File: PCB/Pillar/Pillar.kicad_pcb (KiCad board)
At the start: 2 copper layers, 100 x 86.6 mm, 26 parts, among them CN1 GROVE_IIC_5V, CN2 GROVE_IIC_5V, CN3 USB_A, CN4 AudioJack3_SwitchTR, CN5 Micro_SD_Card_Det_Hirose_DM3AT, J1 Speaker, SW1 MDOE, U1 SeeeduinoXIAO, U2 DFPlayerMini, U3 OLED_128x64_IIC

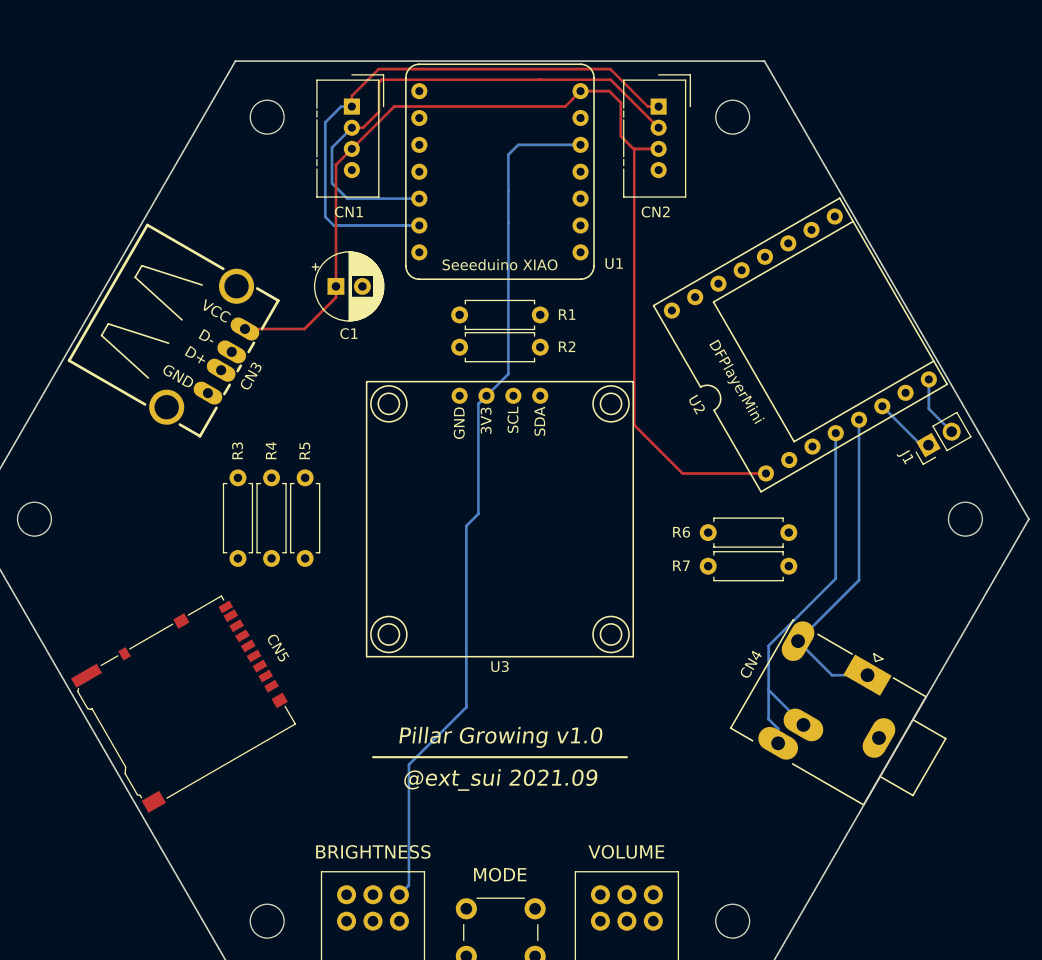
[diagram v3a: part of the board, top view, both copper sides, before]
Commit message: (Pcb) OLED, XIAO のフットプリントに情報を追加して位置を再調整 #60
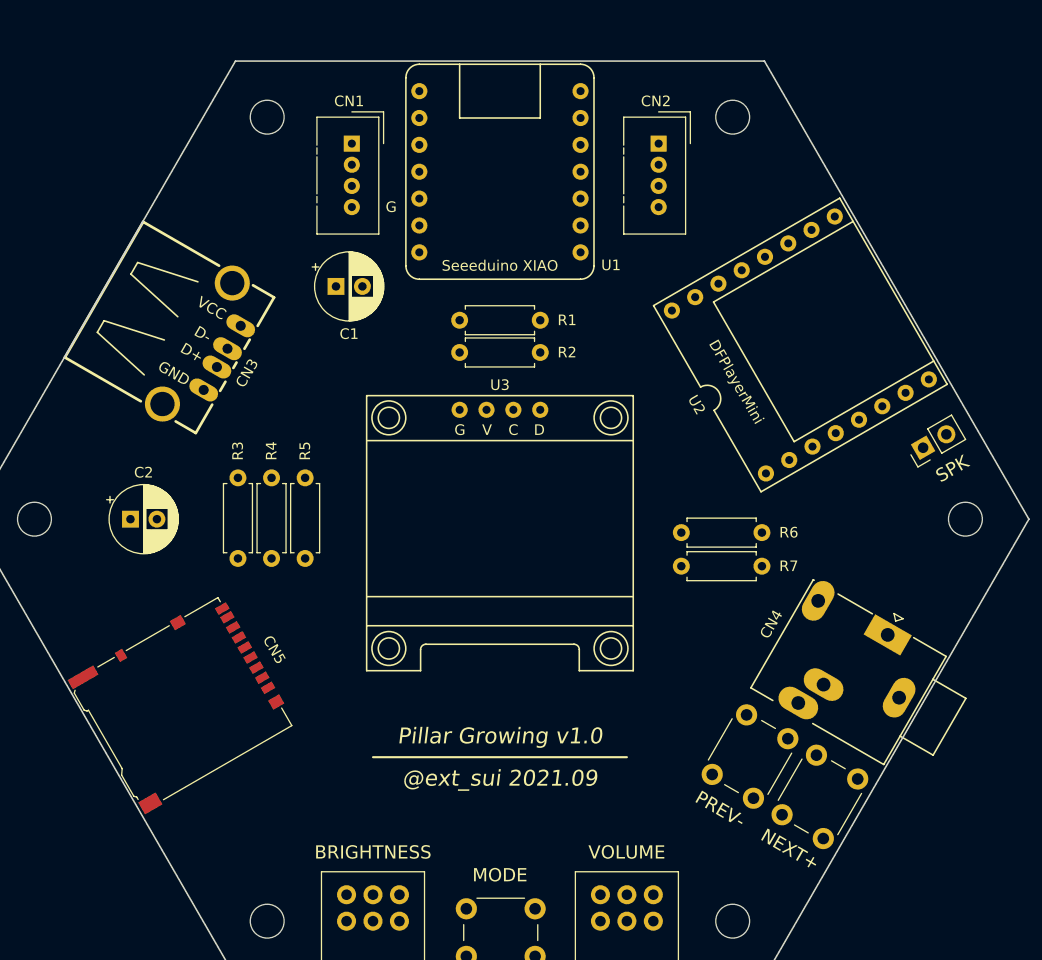
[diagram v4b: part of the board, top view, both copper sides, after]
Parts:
- added C2: 100u, Capacitor_THT:CP_Radial_D6.3mm_P2.50mm, F.Cu at (95.1, 105.0)
- added SW2: NEXT/VOL+, Button_Switch_THT:SW_PUSH_6mm_H8.5mm, F.Cu at (156.7, 132.9)
- added SW3: PREV/VOL-, Button_Switch_THT:SW_PUSH_6mm_H8.5mm, F.Cu at (150.1, 129.1)
- moved CN4 4.26 mm to (166.7, 115.9)
- moved CN1 3.50 mm to (116.0, 69.5)
- moved CN2 3.50 mm to (145.0, 69.5)
- moved R6 2.54 mm to (147.1, 106.3)
- moved R7 2.54 mm to (147.1, 109.4)
- moved U3 1.32 mm to (130.0, 93.3)
- moved J1 0.56 mm to (170.0, 98.2)
- moved R1 0.50 mm to (133.8, 86.2)
- moved R2 0.50 mm to (133.8, 89.2)
- moved CN3 0.50 mm to (101.4, 88.4)
- moved CN5 0.36 mm to (100.0, 122.4)
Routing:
- net 5V: track 100.3 -> 0.00 mm
- net 3V3: track 82.4 -> 0.00 mm
- net SCL: track 53.8 -> 0.00 mm
- net SDA: track 49.3 -> 0.00 mm
- net Net-(CN4-PadR): track 37.0 -> 0.00 mm
- net Net-(CN4-PadT): track 31.2 -> 0.00 mm
- net Net-(J1-Pad1): track 5.88 -> 0.00 mm
- net Net-(J1-Pad2): track 5.83 -> 0.00 mm
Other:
- board text added: "C"
- board text added: "D"
- board text added: "G"
- board text added: "NEXT+"
- board text added: "PREV-"
- board text added: "SPK"
- board text added: "V"
- board text removed: "3V3"
- board text removed: "GND"
- board text removed: "SCL"
- board text removed: "SDA"

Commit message: (Pcb) 配線第0版作成 #60
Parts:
- moved R6 7.62 mm to (154.8, 106.3), turned to 180 degrees
- moved R7 7.62 mm to (154.8, 109.4), turned to 180 degrees
- moved R3 6.35 mm to (111.6, 101.1)
- moved R5 6.35 mm to (105.2, 101.1)
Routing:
- net GND: track 0.00 -> 198.8 mm
- net 3V3: track 0.00 -> 172.6 mm
- net 5V: track 0.00 -> 120.9 mm
- net RV_V: track 0.00 -> 94.7 mm
- net Net-(SW1-Pad1): track 0.00 -> 86.9 mm
- net MOSI: track 0.00 -> 86.6 mm
- net MISO: track 0.00 -> 85.5 mm
- net SCK: track 0.00 -> 75.7 mm, vias 0 -> 1
- net SDA: track 0.00 -> 75.2 mm
- net RV_B: track 0.00 -> 71.4 mm
- net SCL: track 0.00 -> 68.3 mm
- net Net-(SW2-Pad1): track 0.00 -> 66.8 mm
- net Net-(SW3-Pad1): track 0.00 -> 58.6 mm
- net CS: track 0.00 -> 57.1 mm
- net TXD: track 0.00 -> 46.0 mm, vias 0 -> 1
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
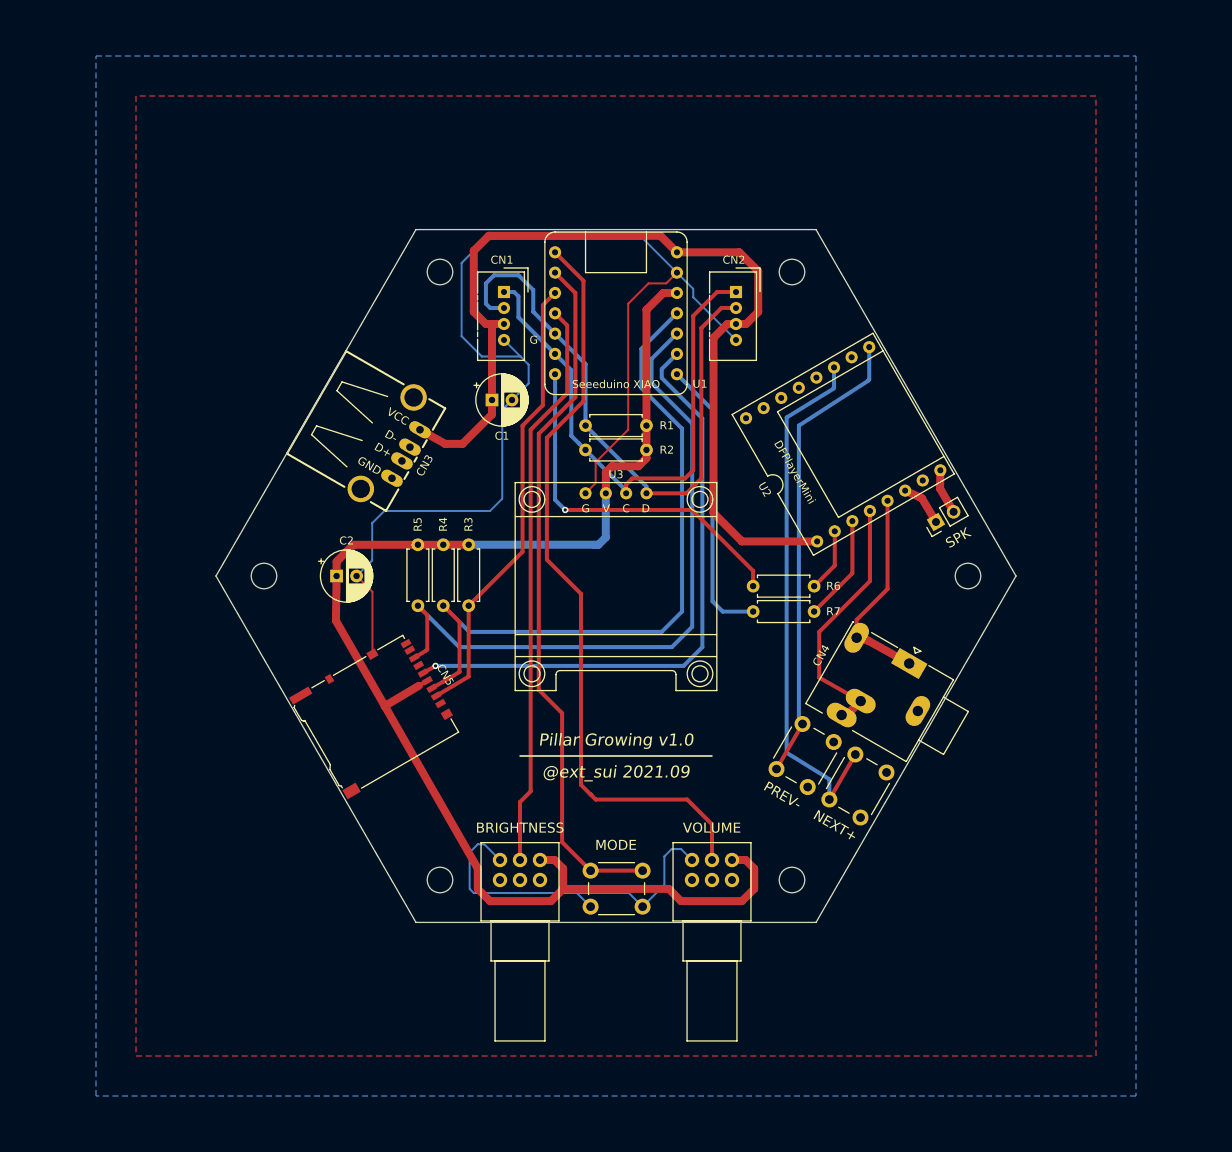
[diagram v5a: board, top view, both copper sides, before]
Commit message: (Pcb) 配線改善：3V3 ラインの直線化と外周 GND 打ち #60
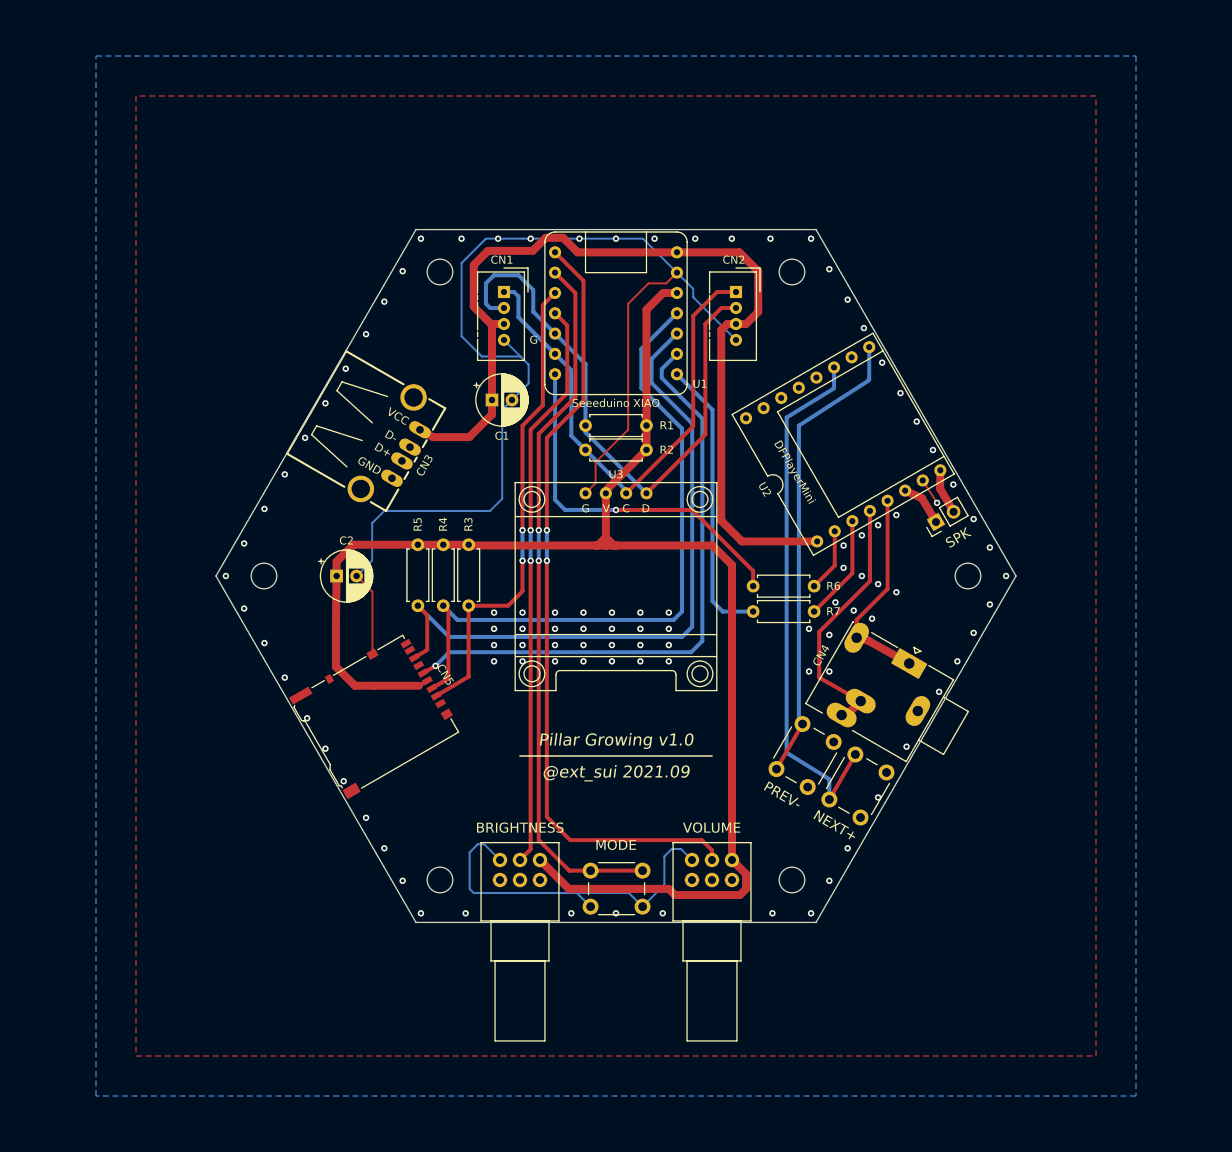
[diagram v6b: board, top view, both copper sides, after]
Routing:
- net 3V3: track 172.6 -> 185.8 mm
- net SCL: track 68.3 -> 64.5 mm
- net GND: track 198.8 -> 202.2 mm, vias 0 -> 100
- net 5V: track 120.9 -> 117.9 mm
- net SDA: track 75.2 -> 72.3 mm
- net RV_V: track 94.7 -> 97.6 mm, vias 0 -> 2
- net CS: track 57.1 -> 60.0 mm, vias 0 -> 2
- net MOSI: track 86.6 -> 84.0 mm
- net Net-(SW1-Pad1): track 86.9 -> 88.4 mm, vias 0 -> 2
- net MISO: track 85.5 -> 84.4 mm
- net RV_B: vias 0 -> 2

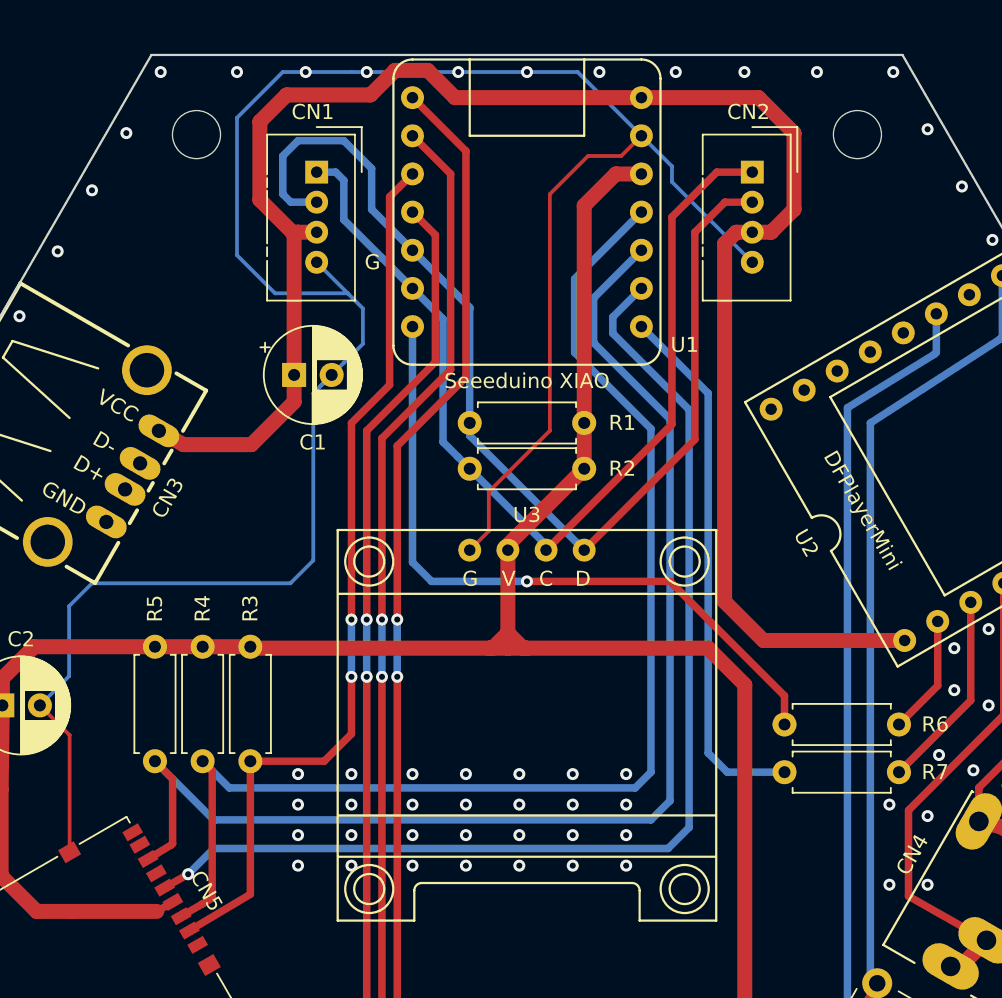
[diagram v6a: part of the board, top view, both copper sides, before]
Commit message: (Pcb) 配線改善：SPI の配線の間に GND ビア打ち #60
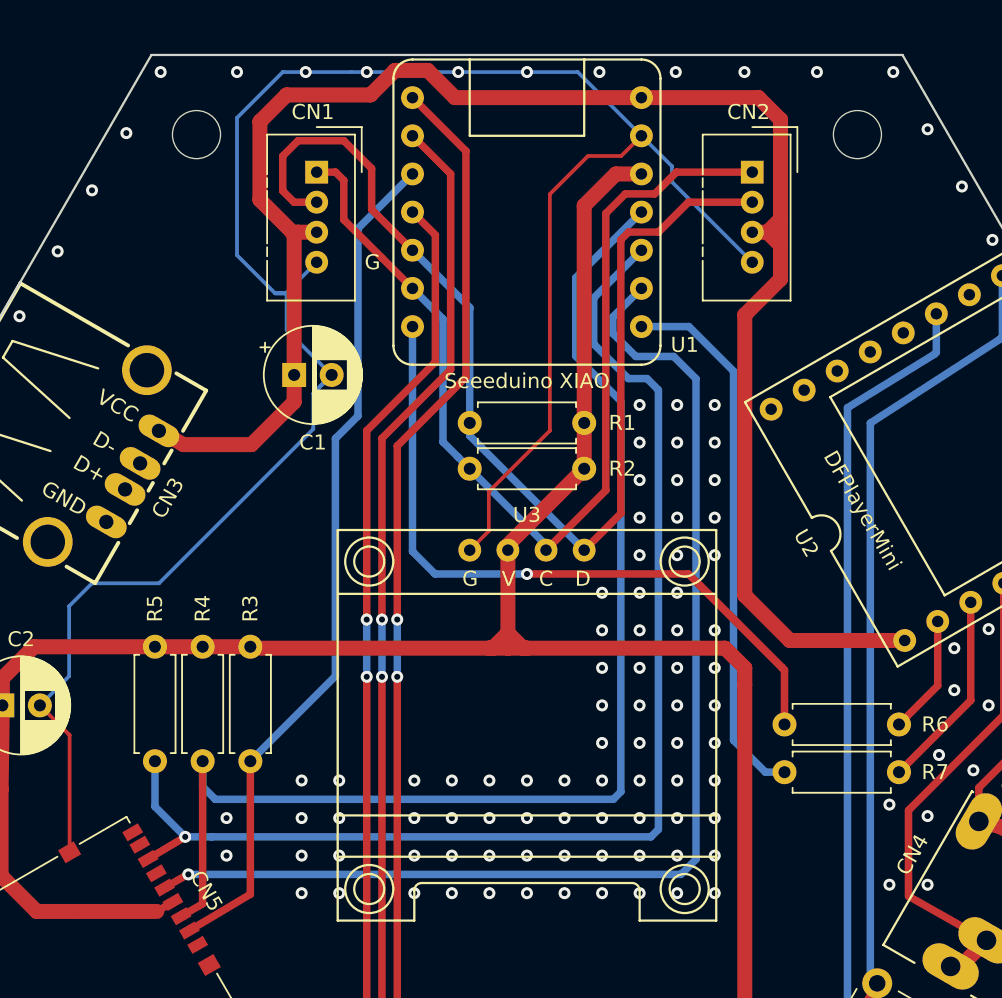
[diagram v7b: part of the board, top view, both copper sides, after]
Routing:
- net TXD: track 46.0 -> 54.8 mm
- net GND: track 202.2 -> 193.6 mm, vias 100 -> 152
- net SCK: track 75.2 -> 78.6 mm
- net CS: track 60.0 -> 57.1 mm, vias 2 -> 0
- net SCL: track 64.5 -> 67.2 mm
- net SDA: track 72.3 -> 74.7 mm
- net MISO: track 84.4 -> 82.8 mm, vias 0 -> 1
- net MOSI: track 84.0 -> 82.9 mm
- net 3V3: track 185.8 -> 186.5 mm

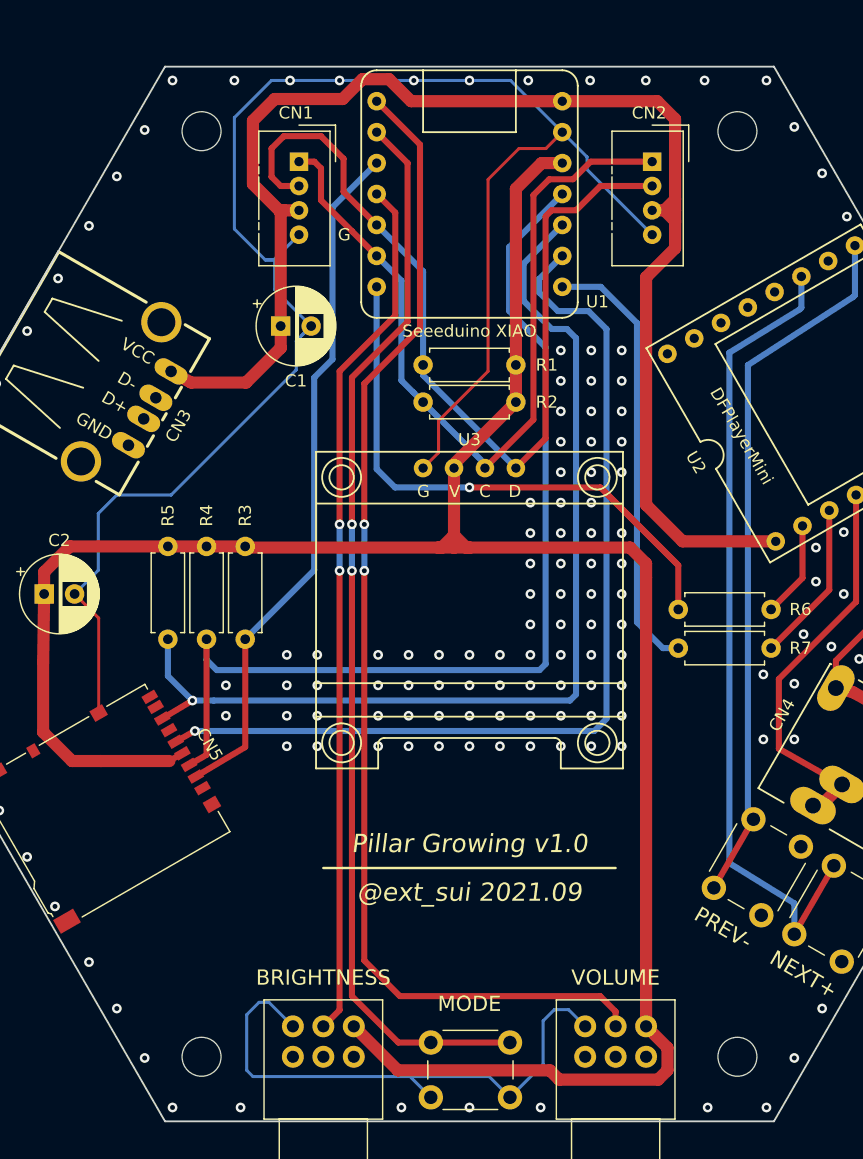
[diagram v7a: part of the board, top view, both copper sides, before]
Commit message: (Pcb) 配線改善：XIAO 周辺の電源と I2C 配線を改善 #60
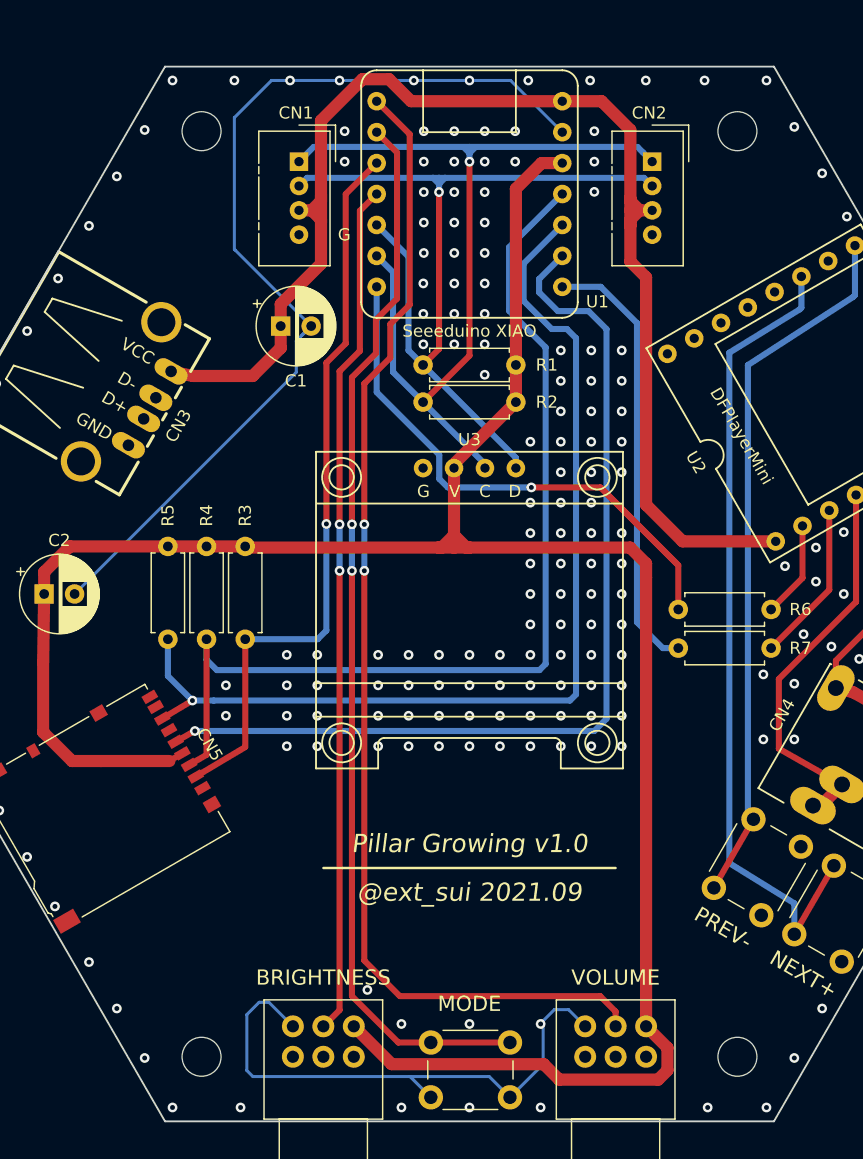
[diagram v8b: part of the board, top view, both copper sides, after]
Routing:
- net GND: track 193.6 -> 131.3 mm, vias 152 -> 190
- net SCL: track 67.2 -> 75.0 mm, vias 0 -> 1
- net 5V: track 118.3 -> 111.0 mm
- net CS: track 57.1 -> 60.6 mm, vias 0 -> 1
- net SDA: track 74.7 -> 71.7 mm, vias 0 -> 1
- net TXD: track 54.8 -> 52.2 mm
- net RV_B: track 71.4 -> 70.2 mm
- net Net-(SW1-Pad1): track 88.4 -> 87.7 mm
- net RV_V: track 97.6 -> 96.9 mm
